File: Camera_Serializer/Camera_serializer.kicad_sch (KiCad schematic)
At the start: 0 parts

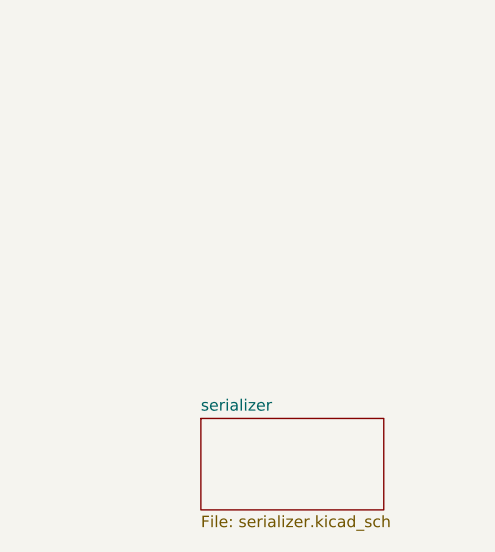
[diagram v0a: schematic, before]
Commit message: Added serializer schematic and fakra connector
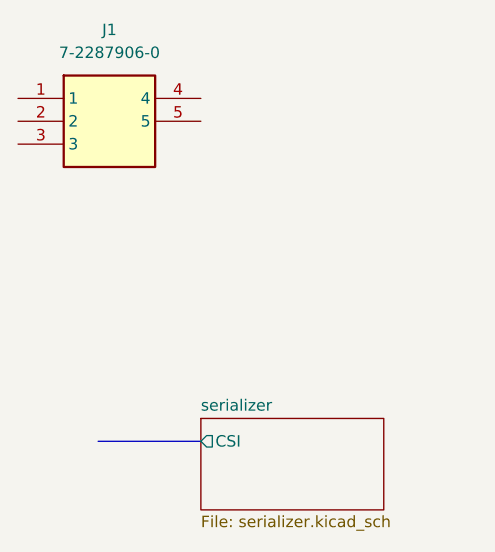
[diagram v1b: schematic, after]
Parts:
- added J1: 7-2287906-0, 7-2287906-0:722879060, symbol 7-2287906-0:7-2287906-0
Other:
- sheet serializer ports: added CSI; removed none

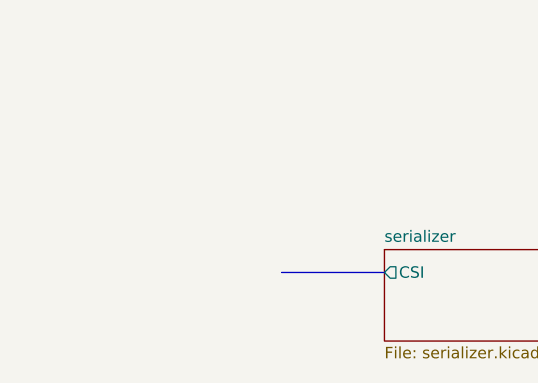
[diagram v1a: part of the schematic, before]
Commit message: Basic setup of main SOC done, working on POC circuit now.
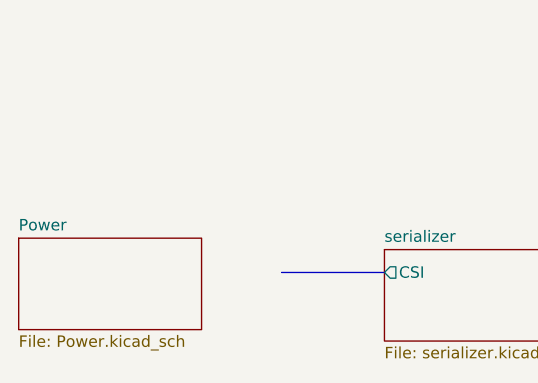
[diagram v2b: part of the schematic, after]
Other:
- added sheet Power (Power.kicad_sch)
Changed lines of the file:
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@@
+		)
+	)
+	(sheet
+		(at 104.14 123.19)
+		(size 20.32 10.16)
+		(fields_autoplaced yes)
+		(stroke
+			(width 0.1524)
+			(type solid)
+		)
+		(fill
+			(color 0 0 0 0.0000)
+		)
+		(property "Sheetname" "Power"
+			(at 104.14 122.4784 0)
+			(effects
+				(font
+					(size 1.27 1.27)
+				)
+				(justify left bottom)
+			)
+		)
+		(property "Sheetfile" "Power.kicad_sch"
+			(at 104.14 133.9346 0)
+			(effects
+				(font
+					(size 1.27 1.27)
+				)
+				(justify left top)
+			)
+		)
+		(instances
+			(project "Camera_serializer"
+				(path "/ebaf1619-da94-4b8e-b57a-a386470e666e"
+					(page "3")
+				)
+			)
 		)
 	)

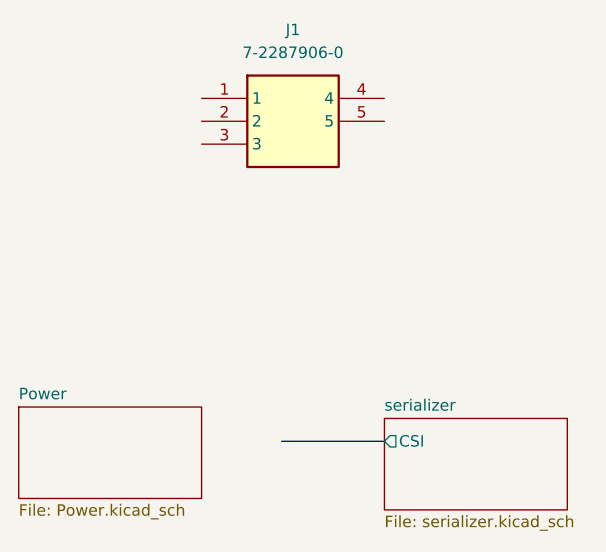
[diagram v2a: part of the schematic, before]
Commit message: Finished POC circuit and added TVS diode
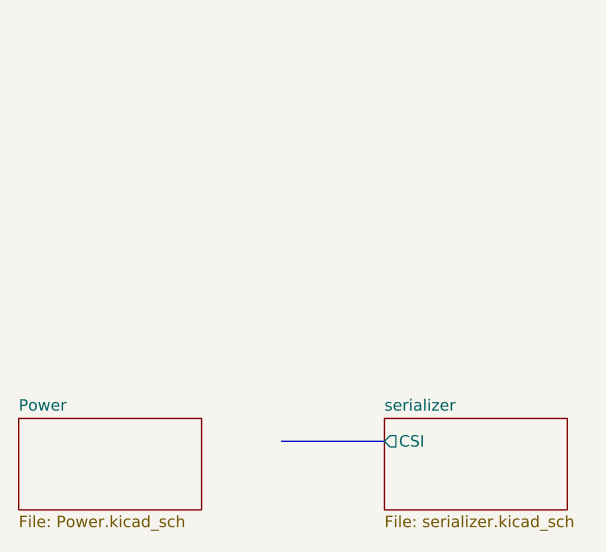
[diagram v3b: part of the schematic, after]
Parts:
- removed J1: 7-2287906-0, 7-2287906-0:722879060, symbol 7-2287906-0:7-2287906-0
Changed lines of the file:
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@@
-		)
-	)
-	(symbol
-		(lib_id "7-2287906-0:7-2287906-0")
-		(at 124.46 88.9 0)
-		(unit 1)
-		(exclude_from_sim no)
-		(in_bom yes)
-		(on_board yes)
-		(dnp no)
-		(fields_autoplaced yes)
-		(property "Reference" "J1"
-			(at 134.62 81.28 0)
-			(effects
-				(font
-					(size 1.27 1.27)
-				)
-			)
-		)
-		(property "Value" "7-2287906-0"
-			(at 134.62 83.82 0)
-			(effects
-				(font
-					(size 1.27 1.27)
-				)
-			)
-		)
-		(property "Footprint" "7-2287906-0:722879060"
-			(at 140.97 183.82 0)
-			(effects
-				(font
-					(size 1.27 1.27)
-				)
-				(justify left top)
-				(hide yes)
-			)
-		)
-		(property "Datasheet" "https://www.mouser.co.uk/datasheet/2/418/6/ENG_CD_2287906_H2-2045594.pdf"
-			(at 140.97 283.82 0)
-			(effects
-				(font
-					(size 1.27 1.27)
-				)
-				(justify left top)
-				(hide yes)
-			)
-		)
-		(property "Description" "Body Features: Connector & Keying Code Z | Body Material PA GF | PCB Retention Feature Plating Material Tin | Configuration Features: PCB Mount Orientation Edge | Number of Positions 1 | Contact Features: Mating Pin Diameter .51 MM | Contact Mating Area Plating Material Gold | Mating Pin Diameter .02 INCH | RF Connector Center Contact Plating Material Gold (Au) | Center Contact With | Contact Type Pin | Dimensions: Product Length .965 INCH | Connector Height .197 INCH | Product Width 7.5 MM | Connector Heig"
-			(at 124.46 88.9 0)
-			(effects
-				(font
-					(size 1.27 1.27)
-				)
-				(hide yes)
-			)
-		)
-		(property "Height" "9.66"
-			(at 140.97 483.82 0)
-			(effects
-				(font
-					(size 1.27 1.27)
-				)
-				(justify left top)
-				(hide yes)
-			)
-		)
-		(property "Manufacturer_Name" "TE Connectivity"
-			(at 140.97 583.82 0)
-			(effects
-				(font
-					(size 1.27 1.27)
-				)
-				(justify left top)
-				(hide yes)
-			)
-		)
-		(property "Manufacturer_Part_Number" "7-2287906-0"
-			(at 140.97 683.82 0)
-			(effects
-				(font
-					(size 1.27 1.27)
-				)
-				(justify left top)
-				(hide yes)
-			)
-		)
-		(property "Mouser Part Number" "571-7-2287906-0"
-			(at 140.97 783.82 0)
-			(effects
-				(font
-					(size 1.27 1.27)
-				)
-				(justify left top)
-				(hide yes)
-			)
-		)
-		(property "Mouser Price/Stock" "https://www.mouser.co.uk/ProductDetail/TE-Connectivity/7-2287906-0?qs=u4fy%2FsgLU9NecSA3FLN8Mg%3D%3D"
-			(at 140.97 883.82 0)
-			(effects
-				(font
-					(size 1.27 1.27)
-				)
-				(justify left top)
-				(hide yes)
-			)
-		)
-		(property "Arrow Part Number" "7-2287906-0"
-			(at 140.97 983.82 0)
-			(effects
-				(font
-					(size 1.27 1.27)
-				)
-				(justify left top)
-				(hide yes)
-			)
-		)
-		(property "Arrow Price/Stock" "https://www.arrow.com/en/products/7-2287906-0/te-connectivity?region=nac"
-			(at 140.97 1083.82 0)
-			(effects
-				(font
-					(size 1.27 1.27)
-				)
-				(justify left top)
-				(hide yes)
-			)
-		)
-		(pin "1"
-		)
-		(pin "2"
-		)
-		(pin "3"
-		)
-		(pin "4"
-		)
-		(pin "5"
-		)
-		(instances
-			(project ""
-				(path "/ebaf1619-da94-4b8e-b57a-a386470e666e"
-					(reference "J1")
-					(unit 1)
-				)
-			)
 		)
 	)
@@
 	)
 	(sheet
-		(at 104.14 123.19)
+		(at 104.14 124.46)
 		(size 20.32 10.16)
 		(fields_autoplaced yes)
@@
 		)
 		(property "Sheetname" "Power"
-			(at 104.14 122.4784 0)
+			(at 104.14 123.7484 0)
 			(effects
 				(font
@@
 		)
 		(property "Sheetfile" "Power.kicad_sch"
-			(at 104.14 133.9346 0)
+			(at 104.14 135.2046 0)
 			(effects
 				(font

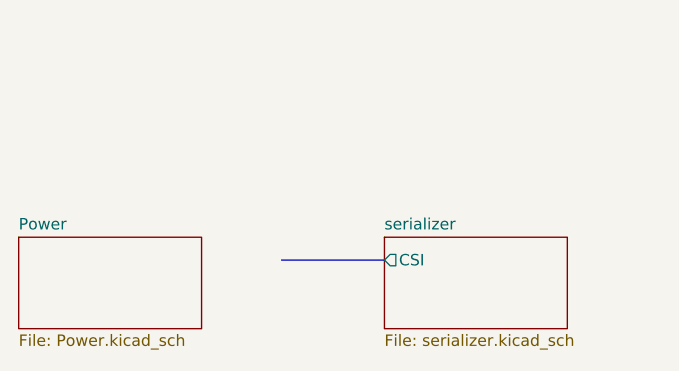
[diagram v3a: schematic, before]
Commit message: Added CSI connector
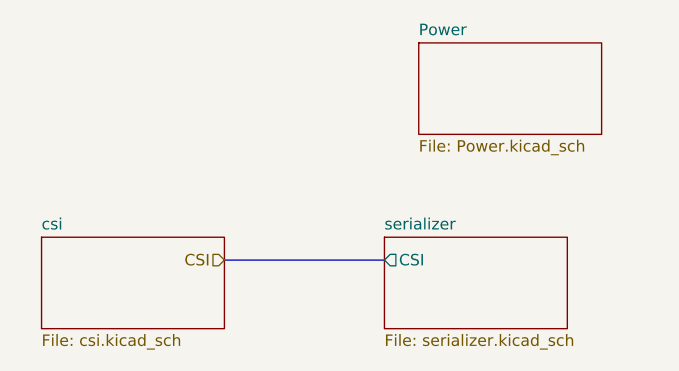
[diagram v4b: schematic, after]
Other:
- added sheet csi (csi.kicad_sch)
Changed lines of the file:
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@@
 	(bus
 		(pts
-			(xy 133.35 127) (xy 144.78 127)
+			(xy 127 127) (xy 144.78 127)
 		)
 		(stroke
 			(width 0)
 			(type default)
+		)
+	)
+	(hierarchical_label "CSI"
+		(shape input)
+		(at 127 127 180)
+		(fields_autoplaced yes)
+		(effects
+			(font
+				(size 1.27 1.27)
+			)
+			(justify right)
 		)
 	)
@@
 	)
 	(sheet
-		(at 104.14 124.46)
+		(at 106.68 124.46)
+		(size 20.32 10.16)
+		(fields_autoplaced yes)
+		(stroke
+			(width 0.1524)
+			(type solid)
+		)
+		(fill
+			(color 0 0 0 0.0000)
+		)
+		(property "Sheetname" "csi"
+			(at 106.68 123.7484 0)
+			(effects
+				(font
+					(size 1.27 1.27)
+				)
+				(justify left bottom)
+			)
+		)
+		(property "Sheetfile" "csi.kicad_sch"
+			(at 106.68 135.2046 0)
+			(effects
+				(font
+					(size 1.27 1.27)
+				)
+				(justify left top)
+			)
+		)
+		(instances
+			(project "Camera_serializer"
+				(path "/ebaf1619-da94-4b8e-b57a-a386470e666e"
+					(page "4")
+				)
+			)
+		)
+	)
+	(sheet
+		(at 148.59 102.87)
 		(size 20.32 10.16)
 		(fields_autoplaced yes)
@@
 		)
 		(property "Sheetname" "Power"
-			(at 104.14 123.7484 0)
+			(at 148.59 102.1584 0)
 			(effects
 				(font
@@
 		)
 		(property "Sheetfile" "Power.kicad_sch"
-			(at 104.14 135.2046 0)
+			(at 148.59 113.6146 0)
 			(effects
 				(font

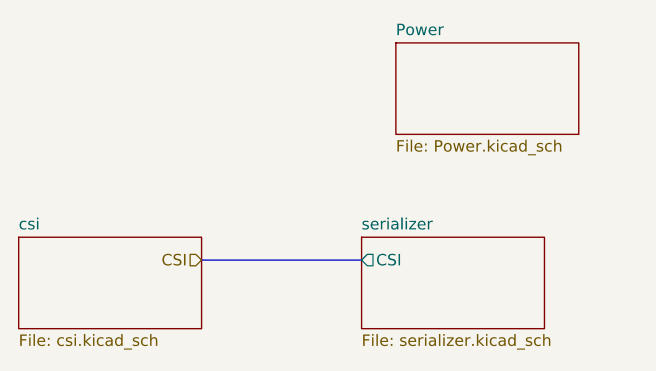
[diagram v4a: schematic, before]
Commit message: Added tvs diodes
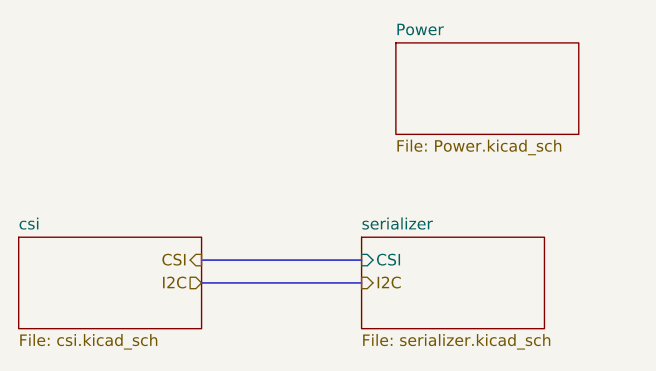
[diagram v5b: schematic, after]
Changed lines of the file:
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@@
+		)
+	)
+	(bus
+		(pts
+			(xy 127 129.54) (xy 144.78 129.54)
+		)
+		(stroke
+			(width 0)
+			(type default)
 		)
 	)
 	(hierarchical_label "CSI"
-		(shape input)
+		(shape output)
 		(at 127 127 180)
 		(fields_autoplaced yes)
@@
 			)
 			(justify right)
+		)
+	)
+	(hierarchical_label "I2C"
+		(shape input)
+		(at 127 129.54 180)
+		(fields_autoplaced yes)
+		(effects
+			(font
+				(size 1.27 1.27)
+			)
+			(justify right)
+		)
+	)
+	(hierarchical_label "I2C"
+		(shape output)
+		(at 144.78 129.54 0)
+		(fields_autoplaced yes)
+		(effects
+			(font
+				(size 1.27 1.27)
+			)
+			(justify left)
 		)
 	)
@@
 			)
 		)
-		(pin "CSI" output
+		(pin "CSI" input
 			(at 144.78 127 180)
 			(effects

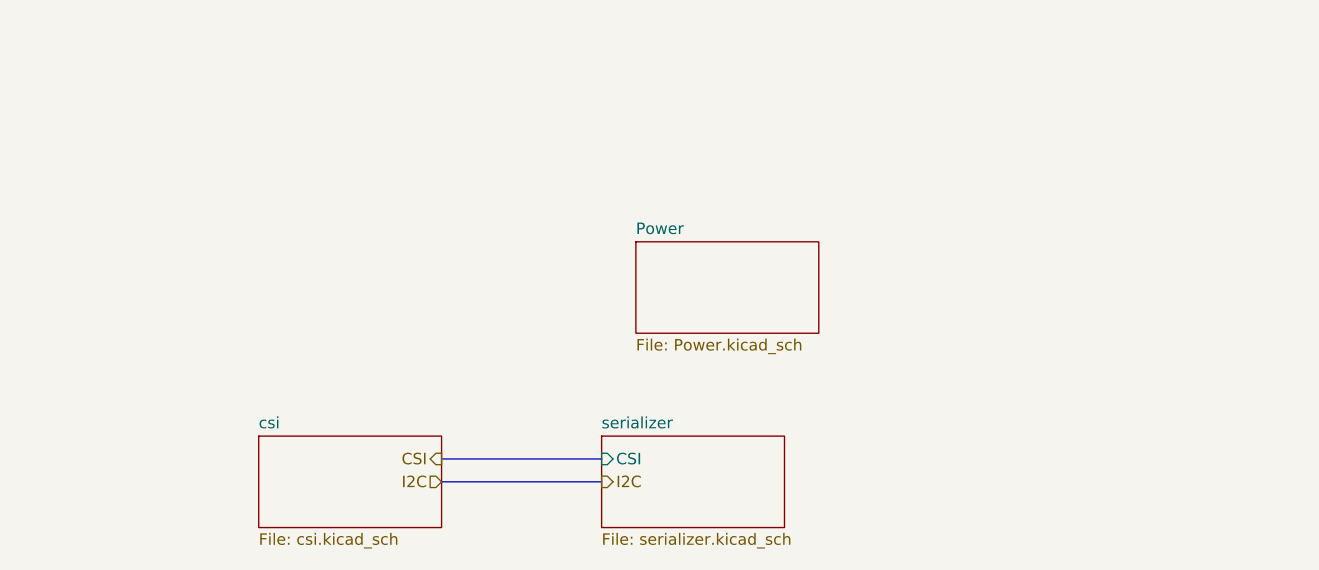
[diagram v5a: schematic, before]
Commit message: Added 5V buck
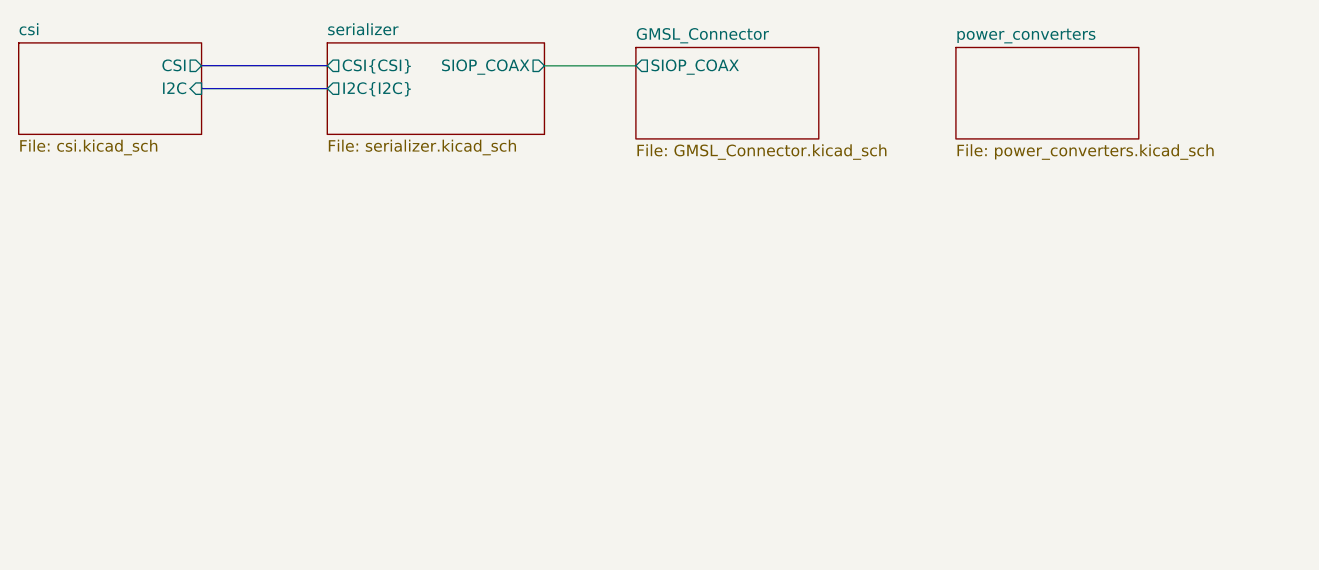
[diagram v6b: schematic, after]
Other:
- sheet Power renamed GMSL_Connector
- added sheet power_converters (power_converters.kicad_sch)
- sheet GMSL_Connector: file Power.kicad_sch -> GMSL_Connector.kicad_sch
- sheet GMSL_Connector ports: added SIOP_COAX; removed none
- sheet csi ports: added CSI, I2C; removed none
- sheet serializer ports: added CSI{CSI}, I2C{I2C}, SIOP_COAX; removed CSI
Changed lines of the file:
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@@
 	(bus
 		(pts
-			(xy 127 127) (xy 144.78 127)
+			(xy 100.33 85.852) (xy 114.3 85.852)
 		)
 		(stroke
@@
 	(bus
 		(pts
-			(xy 127 129.54) (xy 144.78 129.54)
+			(xy 100.33 83.312) (xy 114.3 83.312)
 		)
 		(stroke
@@
 		)
 	)
-	(hierarchical_label "CSI"
-		(shape output)
-		(at 127 127 180)
-		(fields_autoplaced yes)
-		(effects
-			(font
-				(size 1.27 1.27)
-			)
-			(justify right)
-		)
-	)
-	(hierarchical_label "I2C"
-		(shape input)
-		(at 127 129.54 180)
-		(fields_autoplaced yes)
-		(effects
-			(font
-				(size 1.27 1.27)
-			)
-			(justify right)
-		)
-	)
-	(hierarchical_label "I2C"
-		(shape output)
-		(at 144.78 129.54 0)
-		(fields_autoplaced yes)
-		(effects
-			(font
-				(size 1.27 1.27)
-			)
-			(justify left)
-		)
-	)
-	(sheet
-		(at 144.78 124.46)
+	(wire
+		(pts
+			(xy 138.43 83.312) (xy 148.59 83.312)
+		)
+		(stroke
+			(width 0)
+			(type default)
+		)
+	)
+	(sheet
+		(at 114.3 80.772)
+		(size 24.13 10.16)
+		(fields_autoplaced yes)
+		(stroke
+			(width 0.1524)
+			(type solid)
+		)
+		(fill
+			(color 0 0 0 0.0000)
+		)
+		(property "Sheetname" "serializer"
+			(at 114.3 80.0604 0)
+			(effects
+				(font
+					(size 1.27 1.27)
+				)
+				(justify left bottom)
+			)
+		)
+		(property "Sheetfile" "serializer.kicad_sch"
+			(at 114.3 91.5166 0)
+			(effects
+				(font
+					(size 1.27 1.27)
+				)
+				(justify left top)
+			)
+		)
+		(pin "SIOP_COAX" output
+			(at 138.43 83.312 0)
+			(effects
+				(font
+					(size 1.27 1.27)
+				)
+				(justify right)
+			)
+		)
+		(pin "I2C{I2C}" output
+			(at 114.3 85.852 180)
+			(effects
+				(font
+					(size 1.27 1.27)
+				)
+				(justify left)
+			)
+		)
+		(pin "CSI{CSI}" output
+			(at 114.3 83.312 180)
+			(effects
+				(font
+					(size 1.27 1.27)
+				)
+				(justify left)
+			)
+		)
+		(instances
+			(project "Camera_serializer"
+				(path "/ebaf1619-da94-4b8e-b57a-a386470e666e"
+					(page "2")
+				)
+			)
+		)
+	)
+	(sheet
+		(at 80.01 80.772)
 		(size 20.32 10.16)
 		(fields_autoplaced yes)
@@
 			(color 0 0 0 0.0000)
 		)
-		(property "Sheetname" "serializer"
-			(at 144.78 123.7484 0)
-			(effects
-				(font
-					(size 1.27 1.27)
-				)
-				(justify left bottom)
-			)
-		)
-		(property "Sheetfile" "serializer.kicad_sch"
-			(at 144.78 135.2046 0)
-			(effects
-				(font
-					(size 1.27 1.27)
-				)
-				(justify left top)
-			)
-		)
-		(pin "CSI" input
-			(at 144.78 127 180)
+		(property "Sheetname" "csi"
+			(at 80.01 80.0604 0)
+			(effects
+				(font
+					(size 1.27 1.27)
+				)
+				(justify left bottom)
+			)
+		)
+		(property "Sheetfile" "csi.kicad_sch"
+			(at 80.01 91.5166 0)
+			(effects
+				(font
+					(size 1.27 1.27)
+				)
+				(justify left top)
+			)
+		)
+		(pin "CSI" output
+			(at 100.33 83.312 0)
+			(effects
+				(font
+					(size 1.27 1.27)
+				)
+				(justify right)
+			)
+		)
+		(pin "I2C" input
+			(at 100.33 85.852 0)
+			(effects
+				(font
+					(size 1.27 1.27)
+				)
+				(justify right)
+			)
+		)
+		(instances
+			(project "Camera_serializer"
+				(path "/ebaf1619-da94-4b8e-b57a-a386470e666e"
+					(page "4")
+				)
+			)
+		)
+	)
+	(sheet
+		(at 148.59 81.28)
+		(size 20.32 10.16)
+		(fields_autoplaced yes)
+		(stroke
+			(width 0.1524)
+			(type solid)
+		)
+		(fill
+			(color 0 0 0 0.0000)
+		)
+		(property "Sheetname" "GMSL_Connector"
+			(at 148.59 80.5684 0)
+			(effects
+				(font
+					(size 1.27 1.27)
+				)
+				(justify left bottom)
+			)
+		)
+		(property "Sheetfile" "GMSL_Connector.kicad_sch"
+			(at 148.59 92.0246 0)
+			(effects
+				(font
+					(size 1.27 1.27)
+				)
+				(justify left top)
+			)
+		)
+		(pin "SIOP_COAX" output
+			(at 148.59 83.312 180)
 			(effects
 				(font
@@
 			(project "Camera_serializer"
 				(path "/ebaf1619-da94-4b8e-b57a-a386470e666e"
-					(page "2")
-				)
-			)
-		)
-	)
-	(sheet
-		(at 106.68 124.46)
+					(page "3")
+				)
+			)
+		)
+	)
+	(sheet
+		(at 184.15 81.28)
 		(size 20.32 10.16)
 		(fields_autoplaced yes)
@@
 			(color 0 0 0 0.0000)
 		)
-		(property "Sheetname" "csi"
-			(at 106.68 123.7484 0)
-			(effects
-				(font
-					(size 1.27 1.27)
-				)
-				(justify left bottom)
-			)
-		)
-		(property "Sheetfile" "csi.kicad_sch"
-			(at 106.68 135.2046 0)
-			(effects
-				(font
-					(size 1.27 1.27)
-				)
-				(justify left top)
-			)
-		)
-		(instances
-			(project "Camera_serializer"
-				(path "/ebaf1619-da94-4b8e-b57a-a386470e666e"
-					(page "4")
-				)
-			)
-		)
-	)
-	(sheet
-		(at 148.59 102.87)
-		(size 20.32 10.16)
-		(fields_autoplaced yes)
-		(stroke
-			(width 0.1524)
-			(type solid)
-		)
-		(fill
-			(color 0 0 0 0.0000)
-		)
-		(property "Sheetname" "Power"
-			(at 148.59 102.1584 0)
-			(effects
-				(font
-					(size 1.27 1.27)
-				)
-				(justify left bottom)
-			)
-		)
-		(property "Sheetfile" "Power.kicad_sch"
-			(at 148.59 113.6146 0)
-			(effects
-				(font
-					(size 1.27 1.27)
-				)
-				(justify left top)
-			)
-		)
-		(instances
-			(project "Camera_serializer"
-				(path "/ebaf1619-da94-4b8e-b57a-a386470e666e"
-					(page "3")
-				)
-			)
+		(property "Sheetname" "power_converters"
+			(at 184.15 80.5684 0)
+			(effects
+				(font
+					(size 1.27 1.27)
+				)
+				(justify left bottom)
+			)
+		)
+		(property "Sheetfile" "power_converters.kicad_sch"
+			(at 184.15 92.0246 0)
+			(effects
+				(font
+					(size 1.27 1.27)
+				)
+				(justify left top)
+			)
+		)
+		(instances
+			(project "Camera_serializer"
+				(path "/ebaf1619-da94-4b8e-b57a-a386470e666e"
+					(page "5")
+				)
+			)

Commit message: Finishe schematic
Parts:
- added H1, H2, H3, H4: MountingHole_Pad, MountingHole:MountingHole_2.5mm_Pad_Via, symbol Mechanical:MountingHole_Pad
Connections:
- new net GND: H1.1, H2.1, H3.1, H4.1
- no-connect marks 0 -> 3
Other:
- sheet csi ports: added CSI{CSI}, I2C{I2C}; removed CSI, I2C
- sheet serializer ports: added GPIO3, GPIO4, I2C{SDA SCL}, VREF; removed I2C{I2C}

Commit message: Layout started
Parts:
- H1, H2, H3, H4: footprint MountingHole:MountingHole_2.5mm_Pad_Via -> MountingHole:MountingHole_2.5mm_Pad
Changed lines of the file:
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@@
 			)
 		)
-		(property "Footprint" "MountingHole:MountingHole_2.5mm_Pad_Via"
+		(property "Footprint" "MountingHole:MountingHole_2.5mm_Pad"
 			(at 220.98 30.48 0)
 			(effects
@@
 			)
 		)
-		(property "Footprint" "MountingHole:MountingHole_2.5mm_Pad_Via"
+		(property "Footprint" "MountingHole:MountingHole_2.5mm_Pad"
 			(at 220.98 25.4 0)
 			(effects
@@
 			)
 		)
-		(property "Footprint" "MountingHole:MountingHole_2.5mm_Pad_Via"
+		(property "Footprint" "MountingHole:MountingHole_2.5mm_Pad"
 			(at 220.98 20.32 0)
 			(effects
@@
 			)
 		)
-		(property "Footprint" "MountingHole:MountingHole_2.5mm_Pad_Via"
+		(property "Footprint" "MountingHole:MountingHole_2.5mm_Pad"
 			(at 220.98 35.56 0)
 			(effects
